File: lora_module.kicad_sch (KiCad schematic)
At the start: 1 part, among them U1 Ai-Thinker-Ra-02

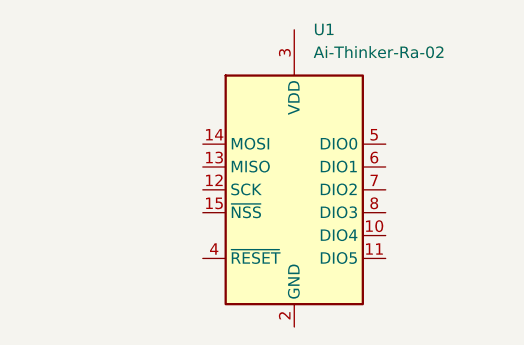
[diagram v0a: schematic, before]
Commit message: feat(LORA_SPI)!: Added Spi communication hierarchical labels to the Lora
Also synced the sheet pins in the root page
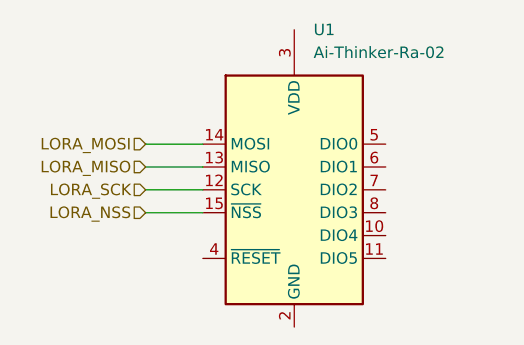
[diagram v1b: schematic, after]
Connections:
- net LORA_SCK: now reaches U1.12 (SCK)
- net LORA_MISO: now reaches U1.13 (MISO)
- net LORA_MOSI: now reaches U1.14 (MOSI)
- net LORA_NSS: now reaches U1.15 (~{NSS})
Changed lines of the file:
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@@
 	(generator_version "9.0")
 	(paper "A4")
+	(wire
+		(pts
+			(xy 129.54 105.41) (xy 135.89 105.41)
+		)
+		(stroke
+			(width 0)
+			(type default)
+		)
+	)
+	(wire
+		(pts
+			(xy 129.54 100.33) (xy 135.89 100.33)
+		)
+		(stroke
+			(width 0)
+			(type default)
+		)
+	)
+	(wire
+		(pts
+			(xy 129.54 97.79) (xy 135.89 97.79)
+		)
+		(stroke
+			(width 0)
+			(type default)
+		)
+	)
+	(wire
+		(pts
+			(xy 129.54 102.87) (xy 135.89 102.87)
+		)
+		(stroke
+			(width 0)
+			(type default)
+		)
+	)
+	(hierarchical_label "LORA_SCK"
+		(shape input)
+		(at 129.54 102.87 180)
+		(effects
+			(font
+				(size 1.27 1.27)
+			)
+			(justify right)
+		)
+	)
+	(hierarchical_label "LORA_MISO"
+		(shape input)
+		(at 129.54 100.33 180)
+		(effects
+			(font
+				(size 1.27 1.27)
+			)
+			(justify right)
+		)
+	)
+	(hierarchical_label "LORA_MOSI"
+		(shape input)
+		(at 129.54 97.79 180)
+		(effects
+			(font
+				(size 1.27 1.27)
+			)
+			(justify right)
+		)
+	)
+	(hierarchical_label "LORA_NSS"
+		(shape input)
+		(at 129.54 105.41 180)
+		(effects
+			(font
+				(size 1.27 1.27)
+			)
+			(justify right)
+		)
+	)
 	(symbol
 		(lib_id "RF_Module:Ai-Thinker-Ra-02")

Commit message: WIP: Save before switching
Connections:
- net RESET: now reaches U1.4 (~{RESET})
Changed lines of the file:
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@@
+	(wire
+		(pts
+			(xy 129.54 110.49) (xy 135.89 110.49)
+		)
+		(stroke
+			(width 0)
+			(type default)
+		)
+	)
 	(wire
 		(pts
@@
 		(effects
 			(font
+				(size 1.27 1.27)
+			)
+			(justify right)
+		)
+	)
+	(hierarchical_label "RESET"
+		(shape input)
+		(at 129.54 110.49 180)
+		(effects
+			(font
